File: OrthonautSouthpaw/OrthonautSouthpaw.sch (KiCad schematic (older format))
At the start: 175 parts, among them K1 7, K10 6, K11 3, K12 ., K13 Tab, K14 Esc, K15 L_Shift, K16 L_Ctrl, K17 Q, K18 A, K19 Z, K2 4, K20 Win, K21 W, K22 S, K23 X, K24 L_Alt, K25 E, K26 D, K27 C, K28 Lower, K29 R, K3 1, K30 F, K31 V, K32 Space, K33 T, K34 G, K35 B, K36 Y, K37 H, K38 N, K39 U, K4 0, K40 J, K41 M, K42 Enter, K43 I, K44 K, K45 ,, K46 Raise, K47 O, K48 L, K49 ., K5 8, K50 R_Alt, K51 P, K52 ;, K53 /, K54 Fn, K55 BackSpace, K56 ', K57 R_Shift, K58 Left, K59 Insert, K6 5, K60 Delete, K61 Up, K62 Down, K63 Home, K64 End, K65 Right, K7 2, K8 00, K9 9, U1 Elite-C

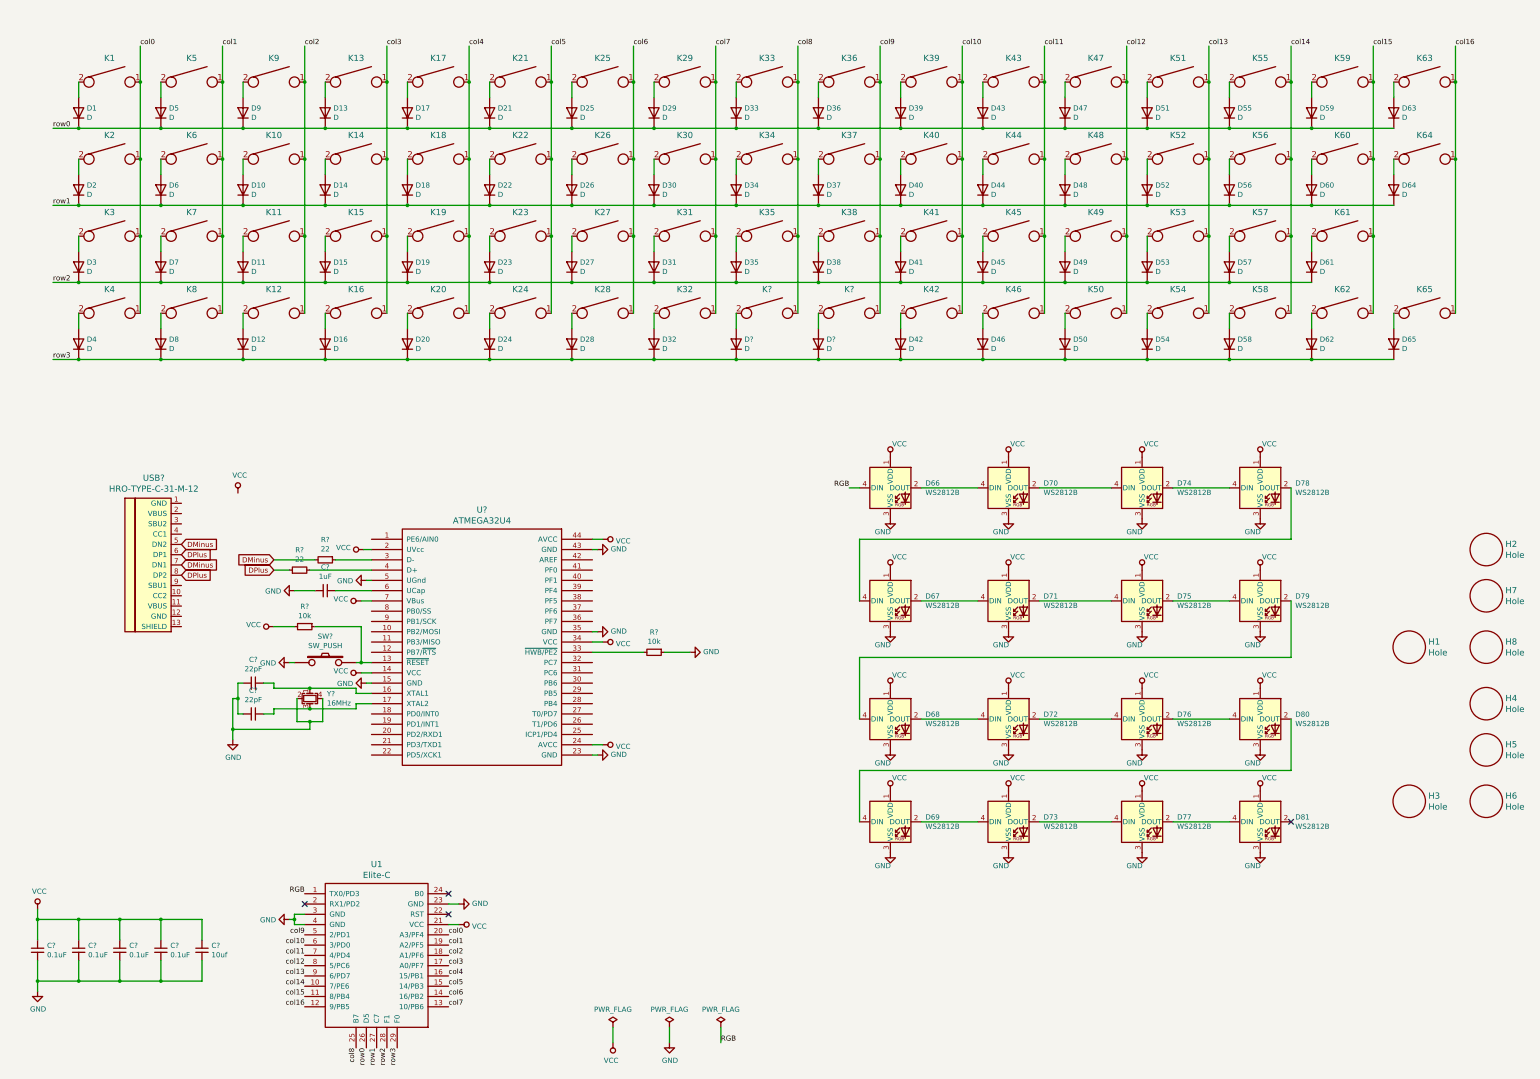
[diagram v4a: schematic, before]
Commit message: 90% done with smd design
all smd components traced except for the rgb legs. need to validate the correct pullthrough design for rgb and need to validate the type c connections
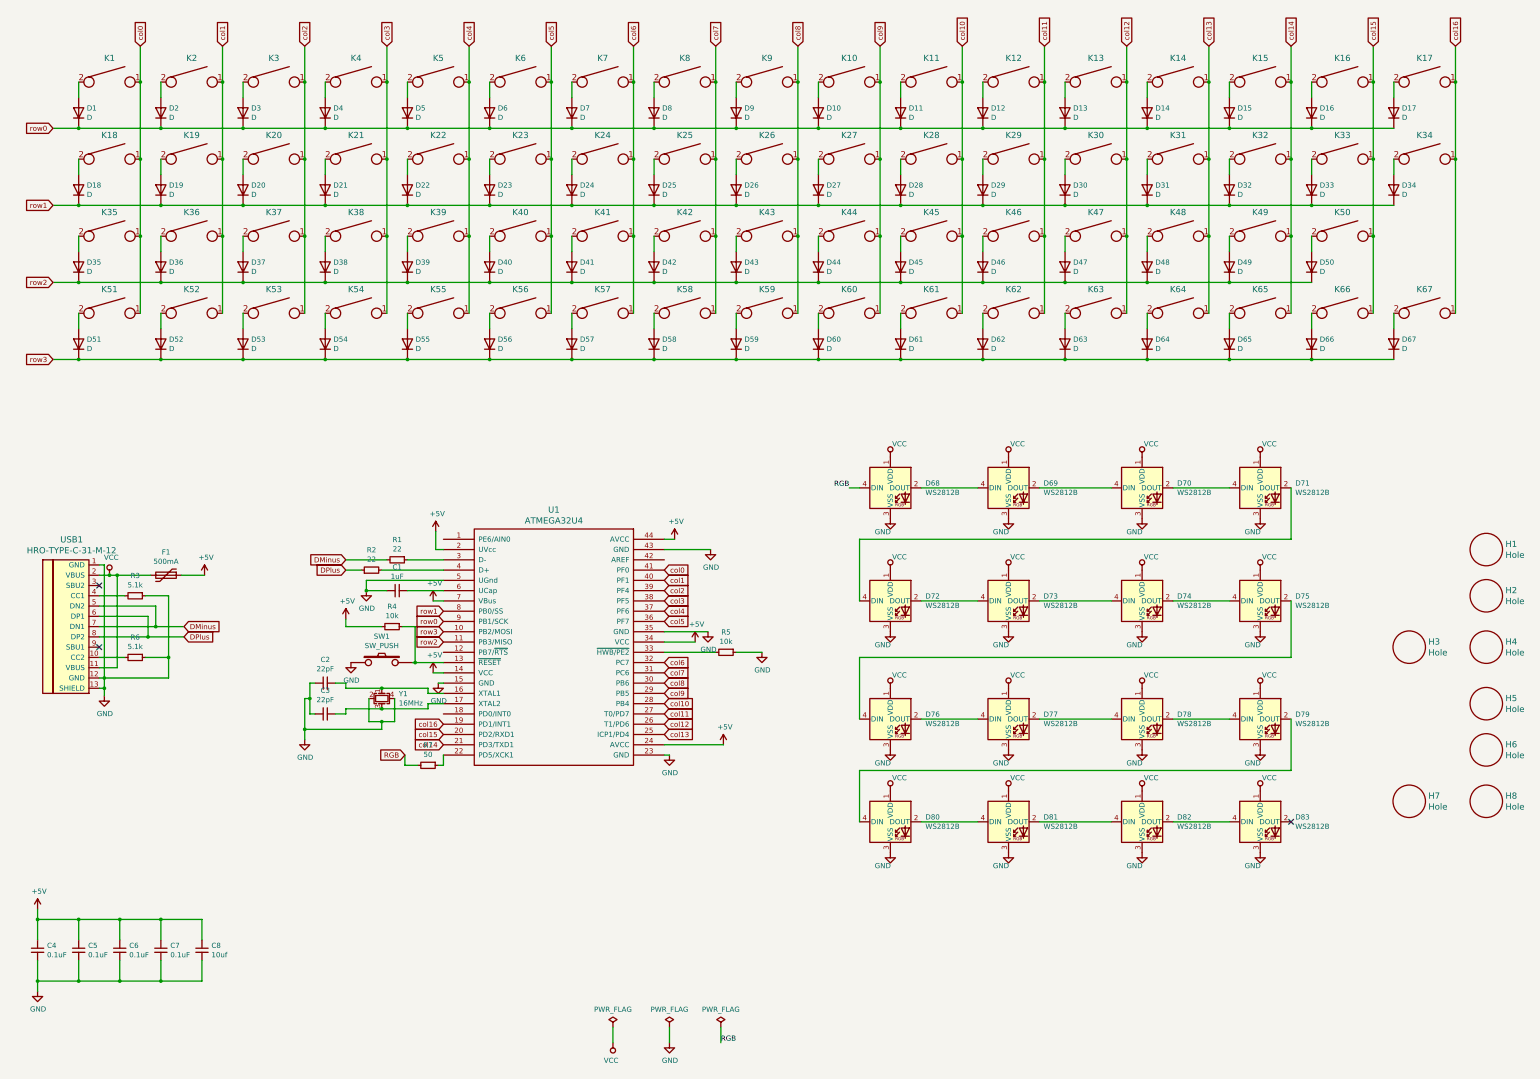
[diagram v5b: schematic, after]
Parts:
- removed U1: Elite-C, Keebio-Parts:Elite-C-ZigZag, symbol keebio:Elite-C
- added F1: 500mA, Fuse_Holders_and_Fuses:Fuse_SMD1206_Reflow, symbol Device:Polyfuse
- added R3, R6: 5.1k, Resistors_SMD:R_0805, symbol Device:R_Small
- added R7: 50, Resistors_SMD:R_0805, symbol Device:R_Small
- C1, C2, C3, C4, C5, C6, C7, C8: renamed from C?; footprint (none) -> Capacitors_SMD:C_0805
- D1: footprint Keebio-Parts:Diode-dual -> Diodes_SMD:D_SOD-123
- D10: renamed from D36; footprint Keebio-Parts:Diode-dual -> Diodes_SMD:D_SOD-123
- D11: renamed from D39; footprint Keebio-Parts:Diode-dual -> Diodes_SMD:D_SOD-123
- D12: renamed from D43; footprint Keebio-Parts:Diode-dual -> Diodes_SMD:D_SOD-123
- D13: renamed from D47; footprint Keebio-Parts:Diode-dual -> Diodes_SMD:D_SOD-123
- D14: renamed from D51; footprint Keebio-Parts:Diode-dual -> Diodes_SMD:D_SOD-123
- D15: renamed from D55; footprint Keebio-Parts:Diode-dual -> Diodes_SMD:D_SOD-123
- D16: renamed from D59; footprint Keebio-Parts:Diode-dual -> Diodes_SMD:D_SOD-123
- D17: renamed from D63; footprint Keebio-Parts:Diode-dual -> Diodes_SMD:D_SOD-123
- D18: renamed from D2; footprint Keebio-Parts:Diode-dual -> Diodes_SMD:D_SOD-123
- D19: renamed from D6; footprint Keebio-Parts:Diode-dual -> Diodes_SMD:D_SOD-123
- D2: renamed from D5; footprint Keebio-Parts:Diode-dual -> Diodes_SMD:D_SOD-123
- D20: renamed from D10; footprint Keebio-Parts:Diode-dual -> Diodes_SMD:D_SOD-123
- D21: renamed from D14; footprint Keebio-Parts:Diode-dual -> Diodes_SMD:D_SOD-123
- D22: renamed from D18; footprint Keebio-Parts:Diode-dual -> Diodes_SMD:D_SOD-123
- D23: renamed from D22; footprint Keebio-Parts:Diode-dual -> Diodes_SMD:D_SOD-123
- D24: renamed from D26; footprint Keebio-Parts:Diode-dual -> Diodes_SMD:D_SOD-123
- D25: renamed from D30; footprint Keebio-Parts:Diode-dual -> Diodes_SMD:D_SOD-123
- D26: renamed from D34; footprint Keebio-Parts:Diode-dual -> Diodes_SMD:D_SOD-123
- D27: renamed from D37; footprint Keebio-Parts:Diode-dual -> Diodes_SMD:D_SOD-123
- D28: renamed from D40; footprint Keebio-Parts:Diode-dual -> Diodes_SMD:D_SOD-123
- D29: renamed from D44; footprint Keebio-Parts:Diode-dual -> Diodes_SMD:D_SOD-123
- D3: renamed from D9; footprint Keebio-Parts:Diode-dual -> Diodes_SMD:D_SOD-123
- D30: renamed from D48; footprint Keebio-Parts:Diode-dual -> Diodes_SMD:D_SOD-123
- D31: renamed from D52; footprint Keebio-Parts:Diode-dual -> Diodes_SMD:D_SOD-123
- D32: renamed from D56; footprint Keebio-Parts:Diode-dual -> Diodes_SMD:D_SOD-123
- D33: renamed from D60; footprint Keebio-Parts:Diode-dual -> Diodes_SMD:D_SOD-123
- D34: renamed from D64; footprint Keebio-Parts:Diode-dual -> Diodes_SMD:D_SOD-123
- D35: renamed from D3; footprint Keebio-Parts:Diode-dual -> Diodes_SMD:D_SOD-123
- D36: renamed from D7; footprint Keebio-Parts:Diode-dual -> Diodes_SMD:D_SOD-123
- D37: renamed from D11; footprint Keebio-Parts:Diode-dual -> Diodes_SMD:D_SOD-123
- D38: renamed from D15; footprint Keebio-Parts:Diode-dual -> Diodes_SMD:D_SOD-123
- D39: renamed from D19; footprint Keebio-Parts:Diode-dual -> Diodes_SMD:D_SOD-123
- D4: renamed from D13; footprint Keebio-Parts:Diode-dual -> Diodes_SMD:D_SOD-123
- D40: renamed from D23; footprint Keebio-Parts:Diode-dual -> Diodes_SMD:D_SOD-123
- D41: renamed from D27; footprint Keebio-Parts:Diode-dual -> Diodes_SMD:D_SOD-123
- D42: renamed from D31; footprint Keebio-Parts:Diode-dual -> Diodes_SMD:D_SOD-123
- D43: renamed from D35; footprint Keebio-Parts:Diode-dual -> Diodes_SMD:D_SOD-123
- D44: renamed from D38; footprint Keebio-Parts:Diode-dual -> Diodes_SMD:D_SOD-123
- D45: renamed from D41; footprint Keebio-Parts:Diode-dual -> Diodes_SMD:D_SOD-123
- D46: renamed from D45; footprint Keebio-Parts:Diode-dual -> Diodes_SMD:D_SOD-123
- D47: renamed from D49; footprint Keebio-Parts:Diode-dual -> Diodes_SMD:D_SOD-123
- D48: renamed from D53; footprint Keebio-Parts:Diode-dual -> Diodes_SMD:D_SOD-123
- D49: renamed from D57; footprint Keebio-Parts:Diode-dual -> Diodes_SMD:D_SOD-123
- D5: renamed from D17; footprint Keebio-Parts:Diode-dual -> Diodes_SMD:D_SOD-123
- D50: renamed from D61; footprint Keebio-Parts:Diode-dual -> Diodes_SMD:D_SOD-123
- D51: renamed from D4; footprint Keebio-Parts:Diode-dual -> Diodes_SMD:D_SOD-123
- D52: renamed from D8; footprint Keebio-Parts:Diode-dual -> Diodes_SMD:D_SOD-123
- D53: renamed from D12; footprint Keebio-Parts:Diode-dual -> Diodes_SMD:D_SOD-123
- D54: renamed from D16; footprint Keebio-Parts:Diode-dual -> Diodes_SMD:D_SOD-123
- D55: renamed from D20; footprint Keebio-Parts:Diode-dual -> Diodes_SMD:D_SOD-123
- D56: renamed from D24; footprint Keebio-Parts:Diode-dual -> Diodes_SMD:D_SOD-123
- D57: renamed from D28; footprint Keebio-Parts:Diode-dual -> Diodes_SMD:D_SOD-123
- D58: renamed from D32; footprint Keebio-Parts:Diode-dual -> Diodes_SMD:D_SOD-123
- D59, D60: renamed from D?; footprint Keebio-Parts:Diode-dual -> Diodes_SMD:D_SOD-123
- D6: renamed from D21; footprint Keebio-Parts:Diode-dual -> Diodes_SMD:D_SOD-123
- D61: renamed from D42; footprint Keebio-Parts:Diode-dual -> Diodes_SMD:D_SOD-123
- D62: renamed from D46; footprint Keebio-Parts:Diode-dual -> Diodes_SMD:D_SOD-123
- D63: renamed from D50; footprint Keebio-Parts:Diode-dual -> Diodes_SMD:D_SOD-123
- D64: renamed from D54; footprint Keebio-Parts:Diode-dual -> Diodes_SMD:D_SOD-123
- D65: renamed from D58; footprint Keebio-Parts:Diode-dual -> Diodes_SMD:D_SOD-123
- D66: renamed from D62; footprint Keebio-Parts:Diode-dual -> Diodes_SMD:D_SOD-123
- D67: renamed from D65; footprint Keebio-Parts:Diode-dual -> Diodes_SMD:D_SOD-123
- D7: renamed from D25; footprint Keebio-Parts:Diode-dual -> Diodes_SMD:D_SOD-123
- D8: renamed from D29; footprint Keebio-Parts:Diode-dual -> Diodes_SMD:D_SOD-123
- D9: renamed from D33; footprint Keebio-Parts:Diode-dual -> Diodes_SMD:D_SOD-123
- K58: renamed from K32; footprint Keebio-Parts:MX_PCB_200H -> Keebio-Parts:MX_PCB_100H
- K59: renamed from K?; value Space -> InnerSpace; footprint Keebio-Parts:MX_PCB_200H -> Keebio-Parts:MX_PCB_100H
- K60: renamed from K?; value Space -> InnerEnter; footprint Keebio-Parts:MX_PCB_200H -> Keebio-Parts:MX_PCB_100H
- K61: renamed from K42; footprint Keebio-Parts:MX_PCB_200H -> Keebio-Parts:MX_PCB_100H
- R1, R2, R4, R5: renamed from R?; footprint (none) -> Resistors_SMD:R_0805
- SW1: renamed from SW?; footprint (none) -> canadian_footprints:SW_TACT_ALPS_SKQGABE010
- U1: renamed from U?; footprint (none) -> Keebio-Parts:ATMEGA32U4-AU
- USB1: renamed from USB?; footprint (none) -> Keebio-Parts:HRO-TYPE-C-31-M-12-Assembly
- Y1: renamed from Y?; footprint (none) -> Crystals:Crystal_SMD_3225-4pin_3.2x2.5mm
- renumbered D66 to D68, D70 to D69, D74 to D70, D78 to D71, D67 to D72, D71 to D73, D75 to D74, D79 to D75, D68 to D76, D72 to D77, D76 to D78, D80 to D79, D69 to D80, D73 to D81, D77 to D82, D81 to D83, H2 to H1, H7 to H2, H1 to H3, H8 to H4, H4 to H5, H5 to H6, H3 to H7, H6 to H8, K36 to K10, K39 to K11, K43 to K12, K47 to K13, K51 to K14, K55 to K15, K59 to K16, K63 to K17, K2 to K18, K6 to K19, K5 to K2, K10 to K20, K14 to K21, K18 to K22, K22 to K23, K26 to K24, K30 to K25, K34 to K26, K37 to K27, K40 to K28, K44 to K29, K9 to K3, K48 to K30, K52 to K31, K56 to K32, K60 to K33, K64 to K34, K3 to K35, K7 to K36, K11 to K37, K15 to K38, K19 to K39, K13 to K4, K23 to K40, K27 to K41, K31 to K42, K35 to K43, K38 to K44, K41 to K45, K45 to K46, K49 to K47, K53 to K48, K57 to K49, K17 to K5, K61 to K50, K4 to K51, K8 to K52, K12 to K53, K16 to K54, K20 to K55, K24 to K56, K28 to K57, K21 to K6, K46 to K62, K50 to K63, K54 to K64, K58 to K65, K62 to K66, K65 to K67, K25 to K7, K29 to K8, K33 to K9
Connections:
- net GND: now also USB1.1 (GND), USB1.12 (GND), USB1.13 (SHIELD), R3.1, R6.1
- net RGB: now also R7.2
- net VCC: now also USB1.11 (VBUS), USB1.2 (VBUS), F1.2; no longer C4.1, C5.1, C6.1, C7.1, C8.1, R4.2, U1.14 (VCC), U1.2 (UVcc), U1.24 (AVCC), U1.34 (VCC), U1.44 (AVCC), U1.7 (VBus)
- net col0: now also U1.41 (PF0)
- net col1: now also U1.40 (PF1)
- net col10: now also U1.28 (PB4)
- net col11: now also U1.27 (T0/PD7)
- net col12: now also U1.26 (T1/PD6)
- net col13: now also U1.25 (ICP1/PD4)
- net col14: now also U1.21 (PD3/TXD1)
- net col15: now also U1.20 (PD2/RXD1)
- net col16: now also U1.19 (PD1/INT1)
- net col2: now also U1.39 (PF4)
- net col3: now also U1.38 (PF5)
- net col4: now also U1.37 (PF6)
- net col5: now also U1.36 (PF7)
- net col6: now also U1.32 (PC7)
- net col7: now also U1.31 (PC6)
- net col8: now also U1.30 (PB6)
- net col9: now also U1.29 (PB5)
- net row0: now also U1.9 (PB1/SCK)
- net row1: now also U1.8 (PB0/SS)
- net row2: now also U1.11 (PB3/MISO)
- net row3: now also U1.10 (PB2/MOSI)
- net at U1.22 (PD5/XCK1): now also R7.1
- net at USB1.10 (CC2): now also R6.2
- net at USB1.4 (CC1): now also R3.2
- new net +5V: C4.1, C5.1, C6.1, C7.1, C8.1, F1.1, R4.2, U1.14 (VCC), U1.2 (UVcc), U1.24 (AVCC), U1.34 (VCC), U1.44 (AVCC), U1.7 (VBus)
- no-connect marks 4 -> 3
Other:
- moved on the sheet: C1, C2, C3, R1, R2, R4, R5, SW1, U1, USB1, Y1
